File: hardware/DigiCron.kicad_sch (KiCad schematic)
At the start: 11 parts, among them J100 Conn_Receptacle_2P, U100 MDBT50Q-U1MV2, U101 HCMS-3917, U102 HCMS-3917, U103 LTR-390UV-01, U104 ADXL345BCCZ-RL, U105 BME280, X100 12401598E4#2A

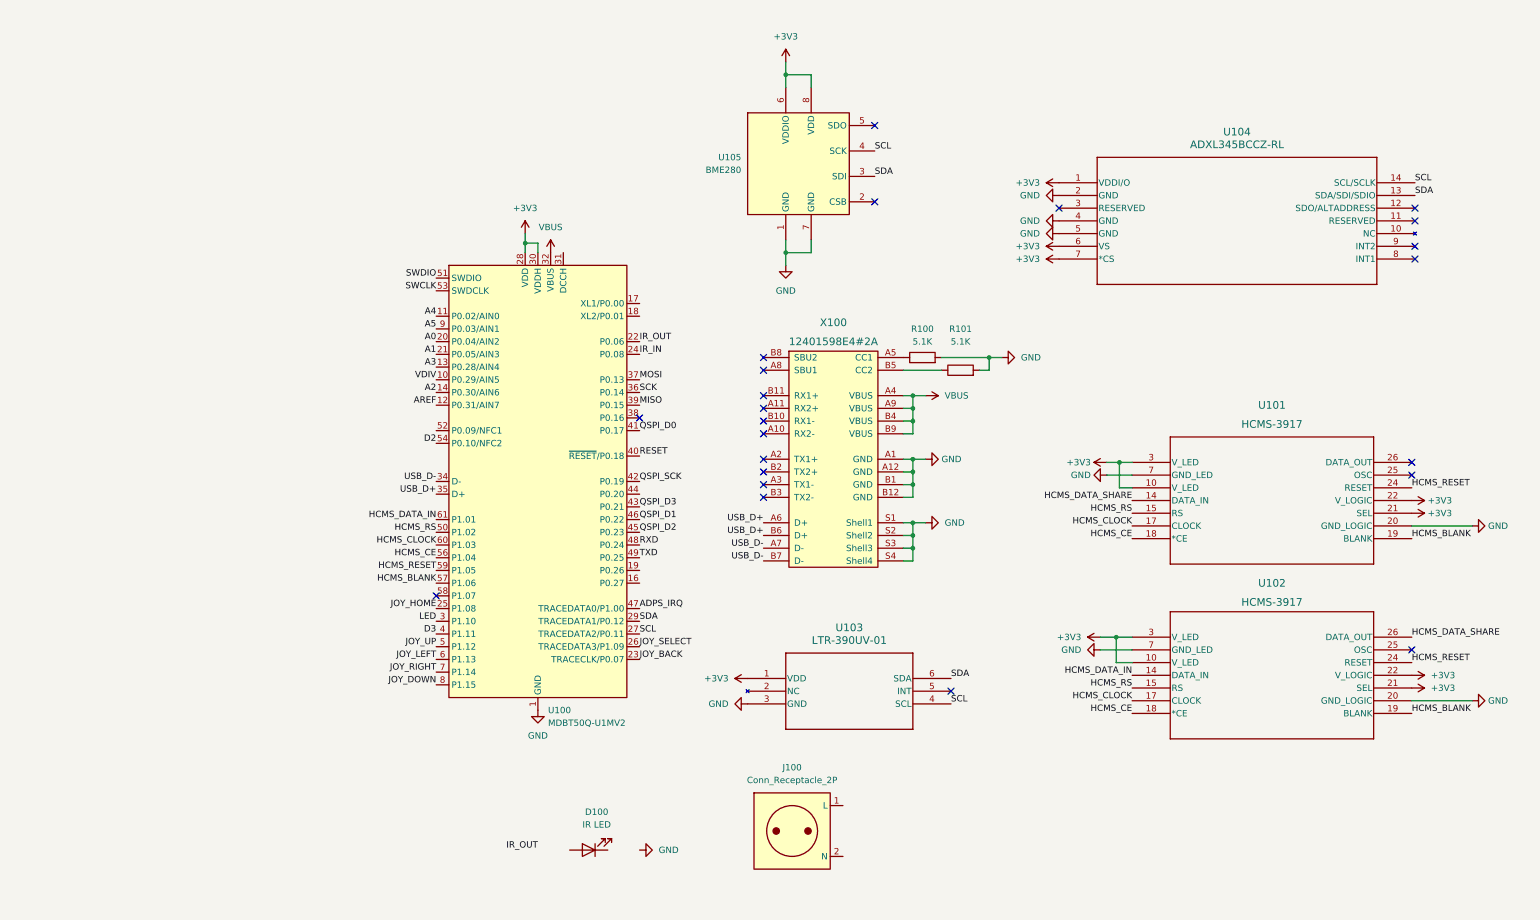
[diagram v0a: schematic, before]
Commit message: Replace displays with 5V versions (due to supply availability) and add power management ICs
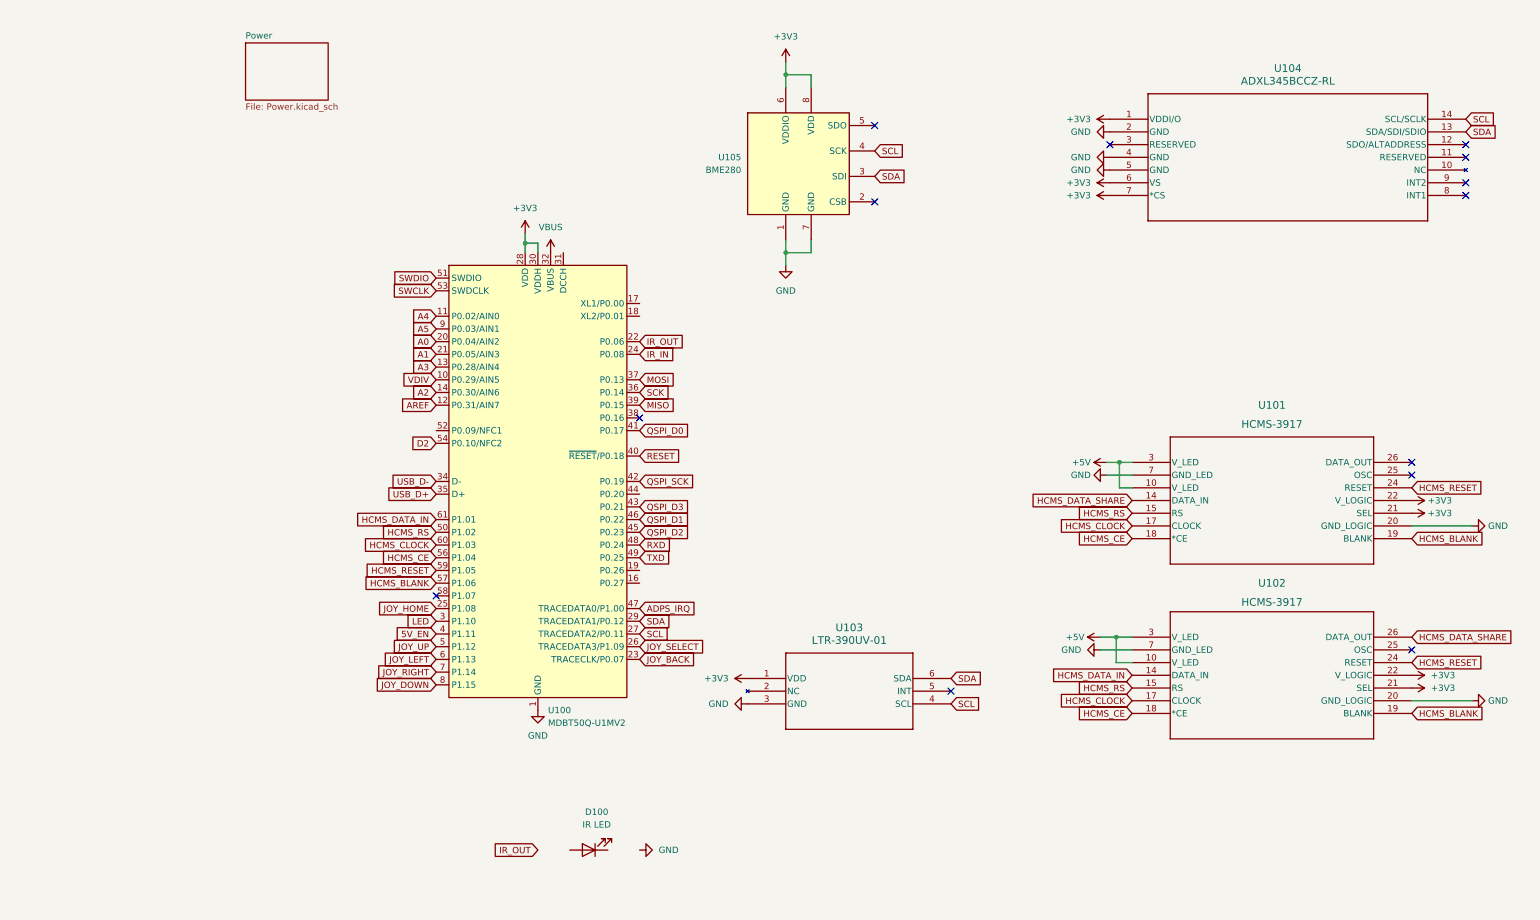
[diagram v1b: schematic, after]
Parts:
- removed J100: Conn_Receptacle_2P, Connector_JST:JST_PH_S2B-PH-SM4-TB_1x02-1MP_P2.00mm_Horizontal, symbol Connector:Conn_Receptacle_2P
- removed R100, R101: 5.1K, Resistor_SMD:R_0201_0603Metric, symbol Device:R
- removed X100: 12401598E4#2A, USB-C:12401598E4#2A, symbol Type-C:12401598E4#2A
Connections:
- net +3V3: no longer U101.10 (V_LED), U101.3 (V_LED), U102.10 (V_LED), U102.3 (V_LED)
- net D3 renamed 5V_EN
- new net +5V: U101.10 (V_LED), U101.3 (V_LED), U102.10 (V_LED), U102.3 (V_LED)
- no-connect marks 23 -> 13
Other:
- added sheet Power (Power.kicad_sch)
- moved on the sheet: U104

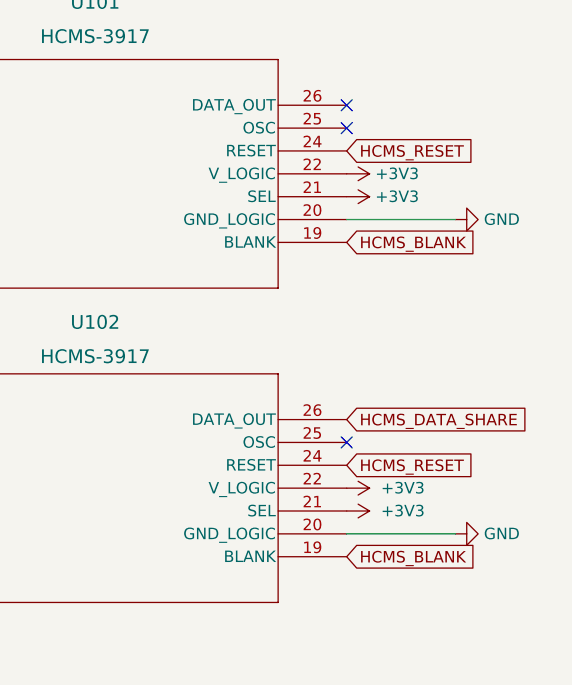
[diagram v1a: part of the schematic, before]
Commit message: Modify 5V boost converter to use VBAT instead of 3V3 for input and add power switching circuit
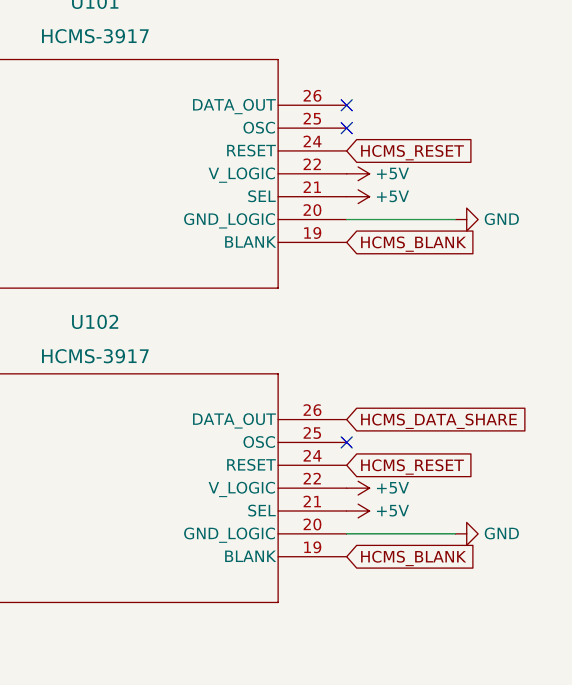
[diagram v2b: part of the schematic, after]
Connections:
- net +3V3: no longer U101.21 (SEL), U101.22 (V_LOGIC), U102.21 (SEL), U102.22 (V_LOGIC)
- net +5V: now also U101.21 (SEL), U101.22 (V_LOGIC), U102.21 (SEL), U102.22 (V_LOGIC)
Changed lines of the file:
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@@
 			)
 		)
-		(property "Value" "+3V3"
-			(at 259.715 145.4149 90)
+		(property "Value" "+5V"
+			(at 259.08 145.4149 90)
 			(effects
 				(font
@@
 			)
 		)
-		(property "Value" "+3V3"
+		(property "Value" "+5V"
 			(at 259.08 110.4899 90)
 			(effects
@@
 			)
 		)
-		(property "Value" "+3V3"
+		(property "Value" "+5V"
 			(at 259.08 113.0299 90)
 			(effects
@@
 			)
 		)
-		(property "Value" "+3V3"
-			(at 259.715 147.9549 90)
-			(effects
-				(font
+		(property "Value" "+5V"
+			(at 259.08 147.9549 90)
+			(effects
+				(font

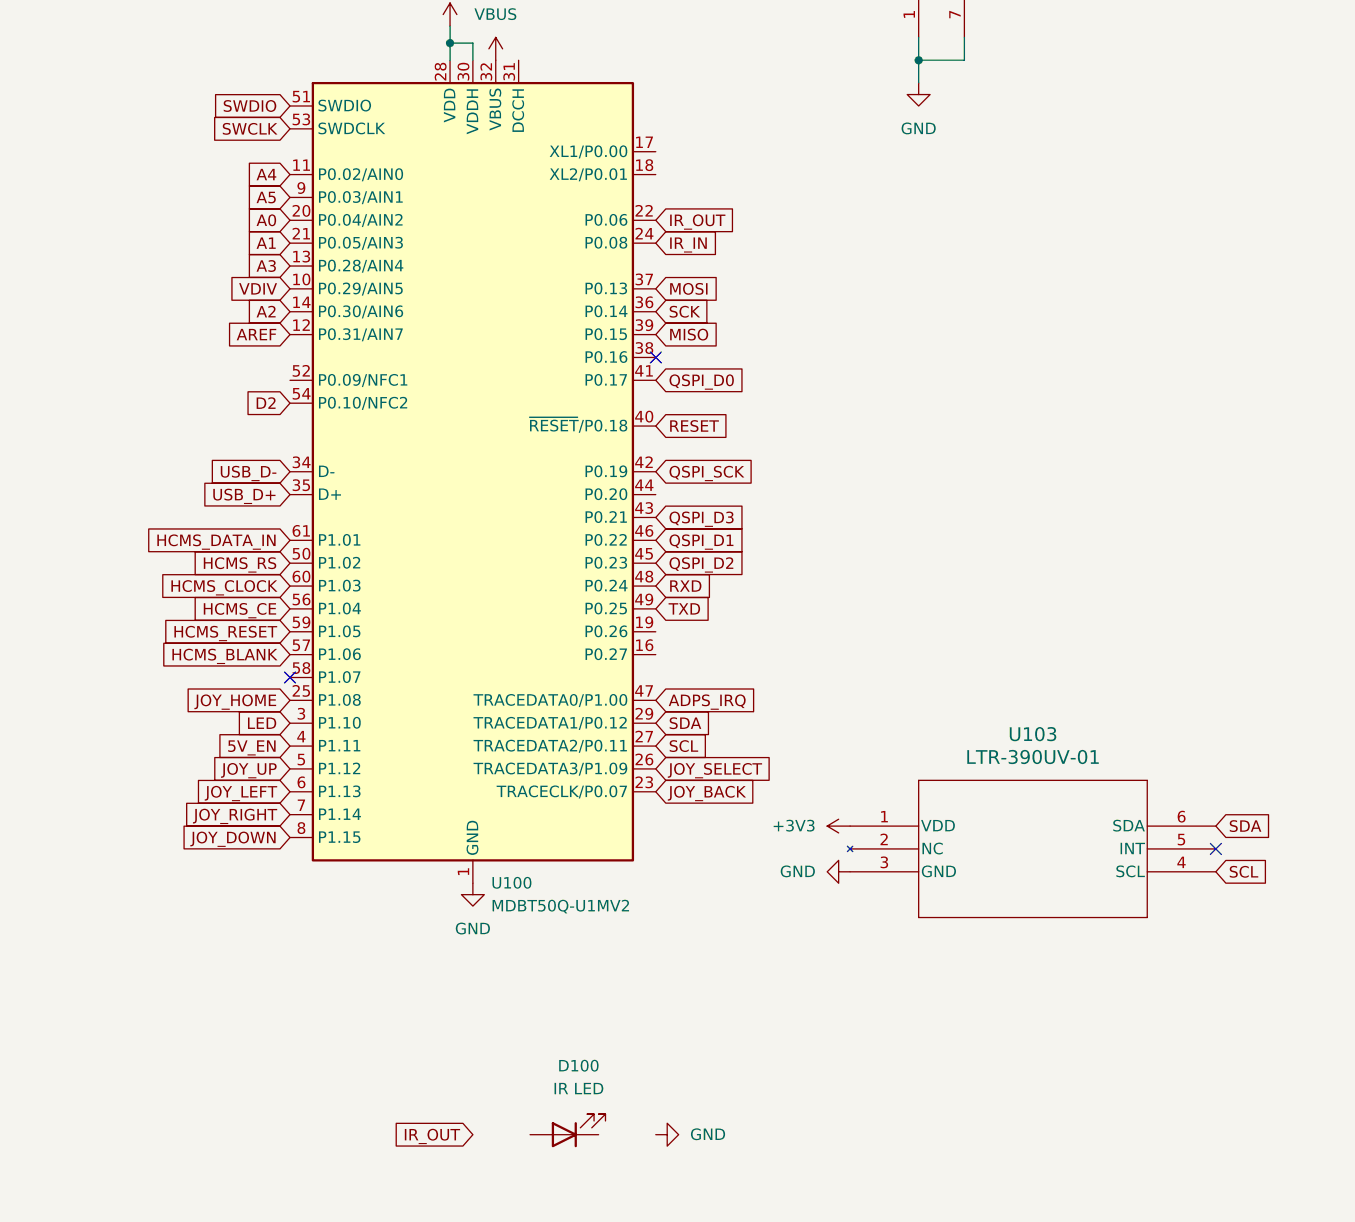
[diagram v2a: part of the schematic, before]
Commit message: Add pads for wiring vibration motor and piezo buzzer
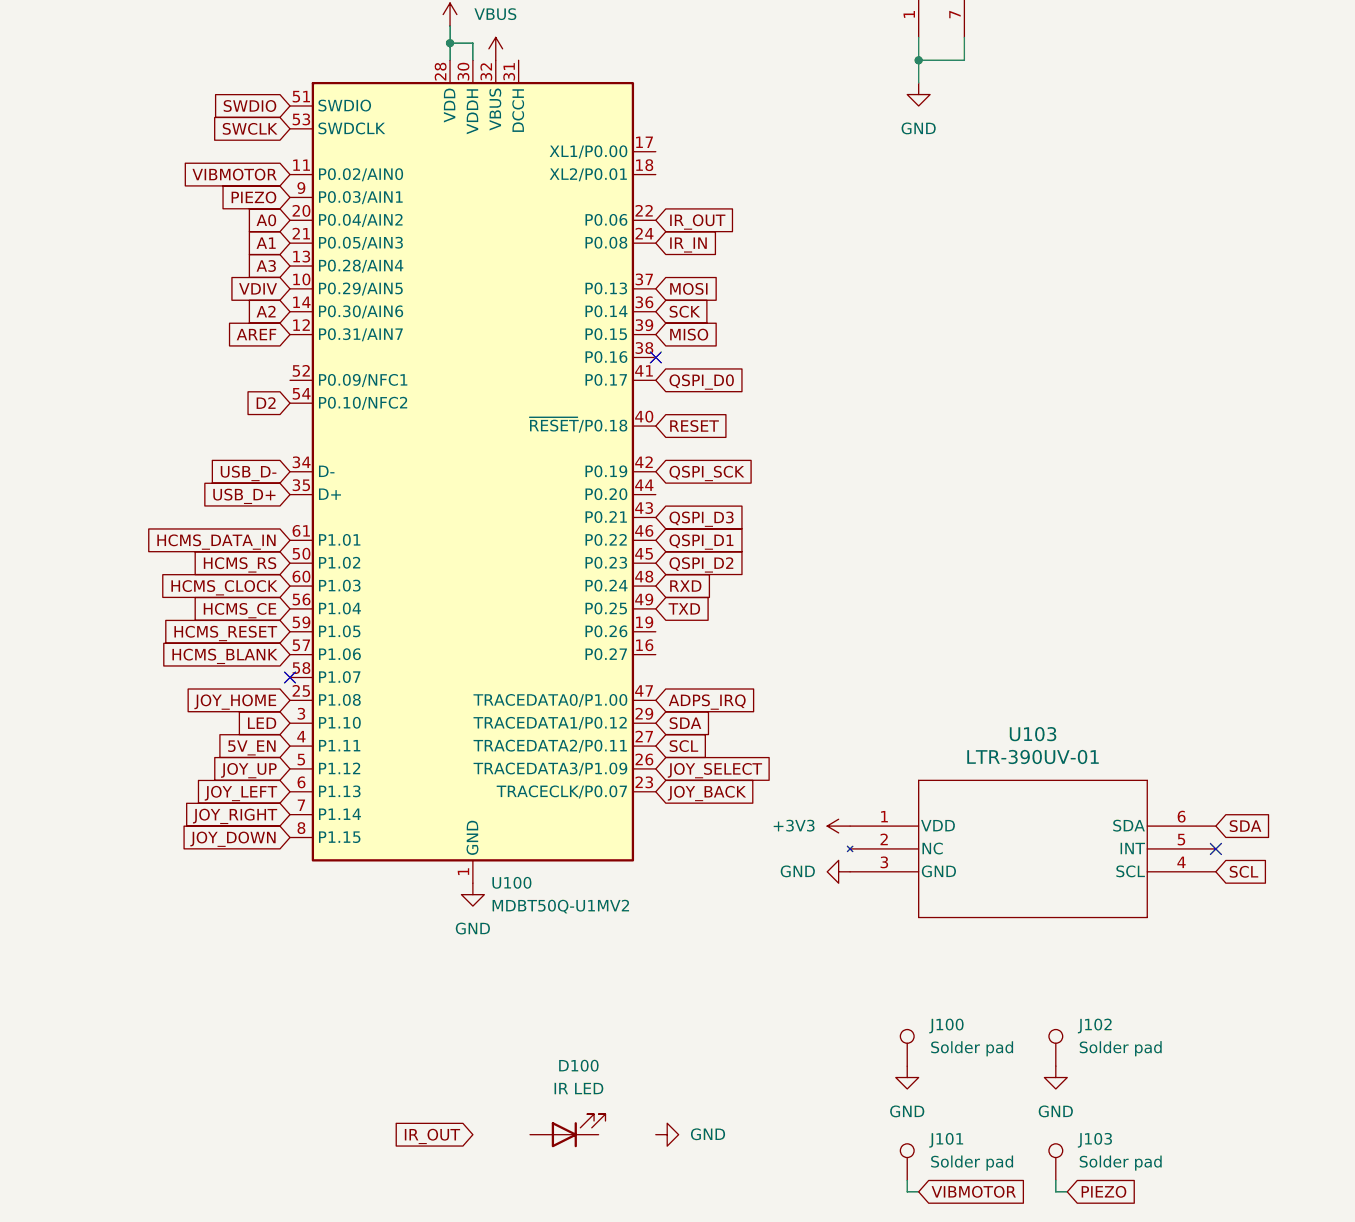
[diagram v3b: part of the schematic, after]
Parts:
- added J100, J101, J102, J103: Solder pad, Connector_Wire:SolderWirePad_1x01_SMD_1x2mm, symbol Connector:TestPoint
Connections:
- net GND: now also J100.1, J102.1
- net A4 renamed VIBMOTOR
- net VIBMOTOR: now also J101.1
- net A5 renamed PIEZO
- net PIEZO: now also J103.1
